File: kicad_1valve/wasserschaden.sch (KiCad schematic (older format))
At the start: 18 parts, among them J1 valve out, J2 12V in, J3 sense, U1 stepdown, U2 WeMos_mini, U3 DS18B20

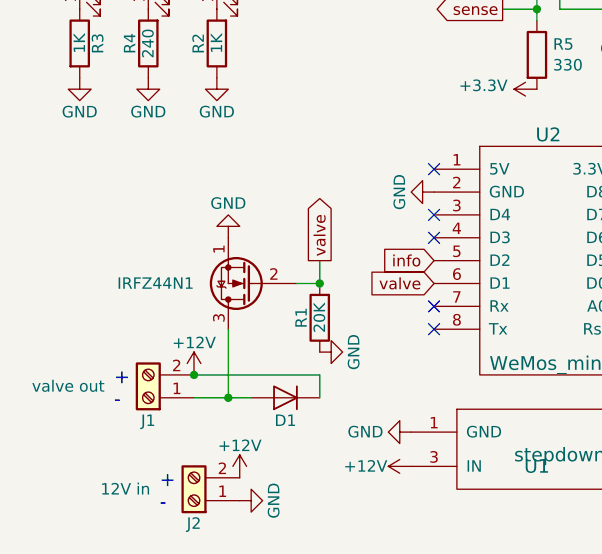
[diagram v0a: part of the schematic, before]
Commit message: use propper symbol and footprint for irlz44n
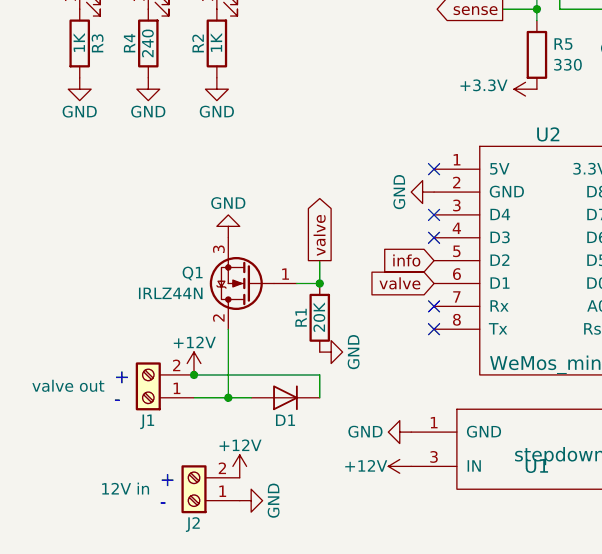
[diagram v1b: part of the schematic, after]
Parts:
- removed IRFZ44N1: (no value), custom:irlz44n_vertical, symbol wasserschaden-cache-2018-10-17-20-35-24:2N7000
- added Q1: IRLZ44N, TO_SOT_Packages_THT:TO-220-3_Vertical, symbol Transistor_FET:IRLZ44N
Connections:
- net GND: now also Q1.3 (S)
- net valve: now also Q1.1 (G)
- net at D1.2 (A), J1.1 (Pin_1): now also Q1.2 (D)
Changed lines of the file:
@@
-$EndComp
-$Comp
-L wasserschaden-cache-2018-10-17-20-35-24:2N7000 IRFZ44N1
-U 1 1 5B2A69C6
-P 2700 2250
-F 0 "IRFZ44N1" H 2950 2250 50  0000 L CNN
-F 1 " " H 2900 2250 50  0000 L CNN
-F 2 "custom:irlz44n_vertical" H 2900 2175 50  0001 L CIN
-F 3 "" H 2700 2250 50  0001 L CNN
-	1    2700 2250
-	-1   0    0    1
 $EndComp
 $Comp
@@
 Text GLabel 4500 2050 2    50   Input ~ 0
 sense
+$Comp
+L Transistor_FET:IRLZ44N Q1
+U 1 1 5DA4CAD4
+P 2700 2250
+F 0 "Q1" H 2906 2204 50  0000 L CNN
+F 1 "IRLZ44N" H 2906 2295 50  0000 L CNN
+F 2 "TO_SOT_Packages_THT:TO-220-3_Vertical" H 2950 2175 50  0001 L CIN
+F 3 "http://www.irf.com/product-info/datasheets/data/irlz44n.pdf" H 2700 2250 50  0001 L CNN
+	1    2700 2250
+	-1   0    0    1
+$EndComp
 $EndSCHEMATC
